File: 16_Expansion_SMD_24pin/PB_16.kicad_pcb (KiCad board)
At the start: 2 copper layers, 148.6 x 75.5 mm, 56 parts, among them J1 String1, J10 String10, J11 String11, J12 String12, J13 String13, J14 String14, J15 String15, J16 String16, J17 Power In Left, J18 Power In Right, J2 String2, J20 v4 Input, J3 String3, J4 String4, J5 String5, J6 String6, J7 String7, J8 String8, J9 String9, U1 74HC245, U2 74HC245

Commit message: added logo
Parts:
- added G***: LOGO, Scotts:chewi_15, F.Cu at (78.4, 112.4)

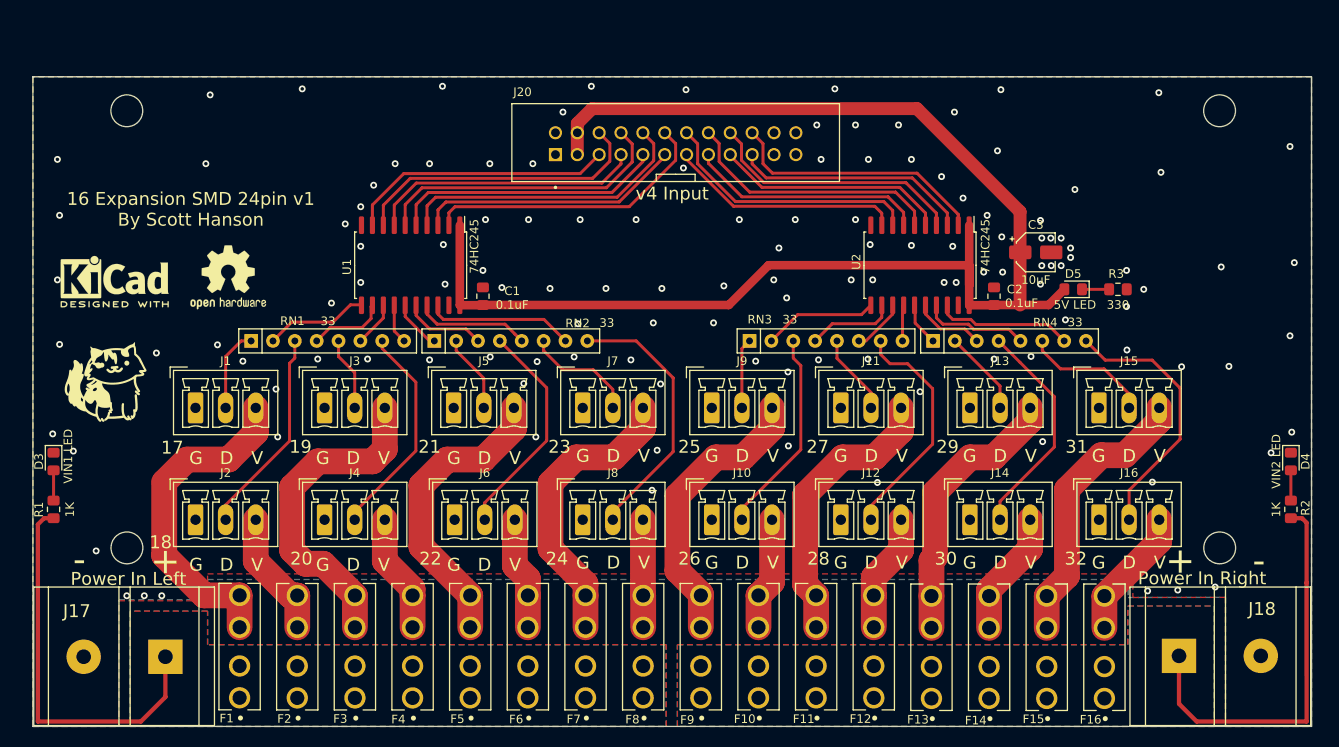
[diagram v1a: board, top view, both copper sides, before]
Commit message: added resistors to help with noise the input lines causing flickering, Updated BOMS
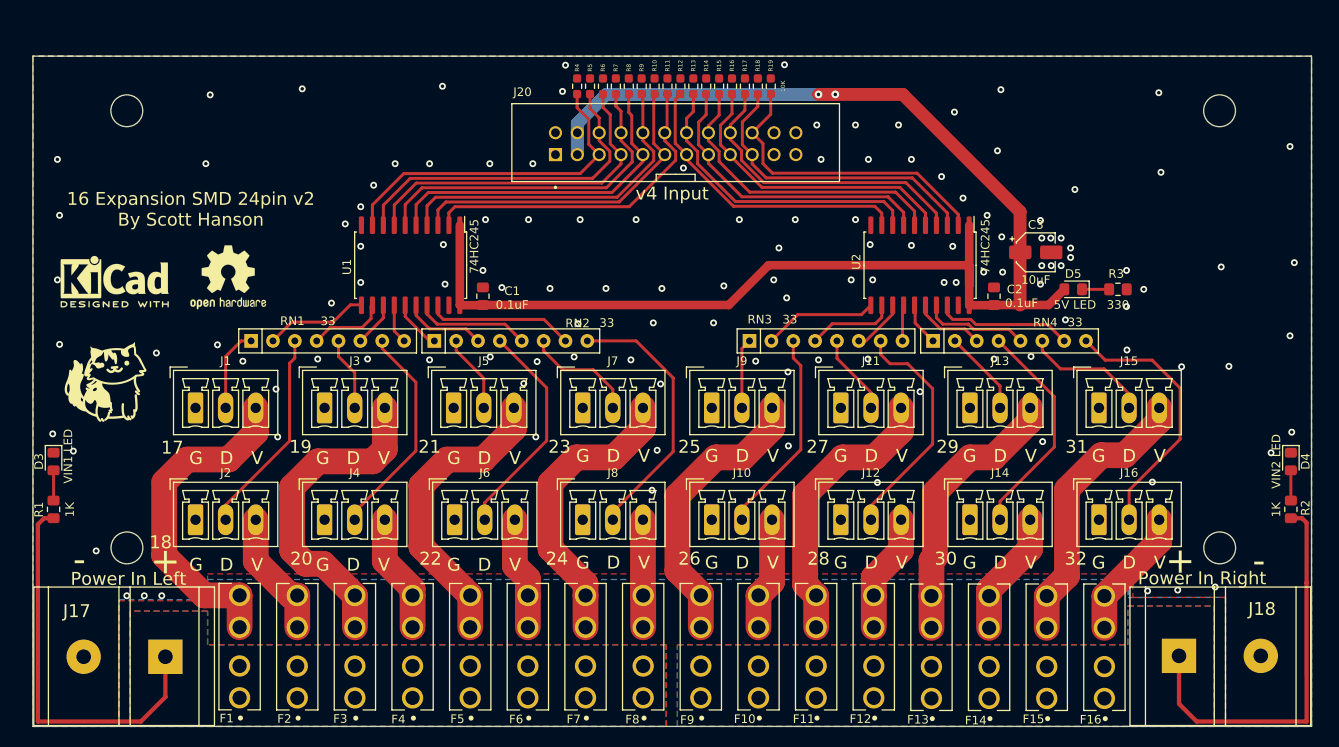
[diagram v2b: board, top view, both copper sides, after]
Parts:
- added R10: 10K, Resistor_SMD:R_0603_1608Metric_Pad0.98x0.95mm_HandSolder, F.Cu at (142.5, 79.2)
- added R11: 10K, Resistor_SMD:R_0603_1608Metric_Pad0.98x0.95mm_HandSolder, F.Cu at (144.0, 79.2)
- added R12: 10K, Resistor_SMD:R_0603_1608Metric_Pad0.98x0.95mm_HandSolder, F.Cu at (145.5, 79.2)
- added R13: 10K, Resistor_SMD:R_0603_1608Metric_Pad0.98x0.95mm_HandSolder, F.Cu at (147.0, 79.2)
- added R14: 10K, Resistor_SMD:R_0603_1608Metric_Pad0.98x0.95mm_HandSolder, F.Cu at (148.5, 79.2)
- added R15: 10K, Resistor_SMD:R_0603_1608Metric_Pad0.98x0.95mm_HandSolder, F.Cu at (150.0, 79.2)
- added R16: 10K, Resistor_SMD:R_0603_1608Metric_Pad0.98x0.95mm_HandSolder, F.Cu at (151.5, 79.2)
- added R17: 10K, Resistor_SMD:R_0603_1608Metric_Pad0.98x0.95mm_HandSolder, F.Cu at (153.0, 79.2)
- added R18: 10K, Resistor_SMD:R_0603_1608Metric_Pad0.98x0.95mm_HandSolder, F.Cu at (154.5, 79.2)
- added R19: 10K, Resistor_SMD:R_0603_1608Metric_Pad0.98x0.95mm_HandSolder, F.Cu at (156.0, 79.2)
- added R4: 10K, Resistor_SMD:R_0603_1608Metric_Pad0.98x0.95mm_HandSolder, F.Cu at (133.5, 79.2)
- added R5: 10K, Resistor_SMD:R_0603_1608Metric_Pad0.98x0.95mm_HandSolder, F.Cu at (135.0, 79.2)
- added R6: 10K, Resistor_SMD:R_0603_1608Metric_Pad0.98x0.95mm_HandSolder, F.Cu at (136.5, 79.2)
- added R7: 10K, Resistor_SMD:R_0603_1608Metric_Pad0.98x0.95mm_HandSolder, F.Cu at (138.0, 79.2)
- added R8: 10K, Resistor_SMD:R_0603_1608Metric_Pad0.98x0.95mm_HandSolder, F.Cu at (139.5, 79.2)
- added R9: 10K, Resistor_SMD:R_0603_1608Metric_Pad0.98x0.95mm_HandSolder, F.Cu at (141.0, 79.2)
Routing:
- net OUT31: track 27.6 -> 35.8 mm
- net OUT17: track 31.1 -> 39.2 mm
- net OUT29: track 27.0 -> 35.0 mm
- net OUT19: track 31.8 -> 39.7 mm
- net OUT27: track 27.6 -> 35.4 mm
- net OUT25: track 27.2 -> 35.1 mm
- net OUT21: track 31.6 -> 39.3 mm
- net OUT23: track 30.9 -> 38.5 mm
- net OUT32: track 30.5 -> 35.9 mm
- net OUT30: track 30.3 -> 35.5 mm
- net OUT28: track 30.6 -> 35.6 mm
- net OUT18: track 34.6 -> 39.5 mm
- net OUT26: track 30.8 -> 35.6 mm
- net OUT20: track 34.8 -> 39.5 mm
- net OUT24: track 34.1 -> 38.7 mm
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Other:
- board size 148.6 x 75.5 mm -> 148.6 x 77.9 mm

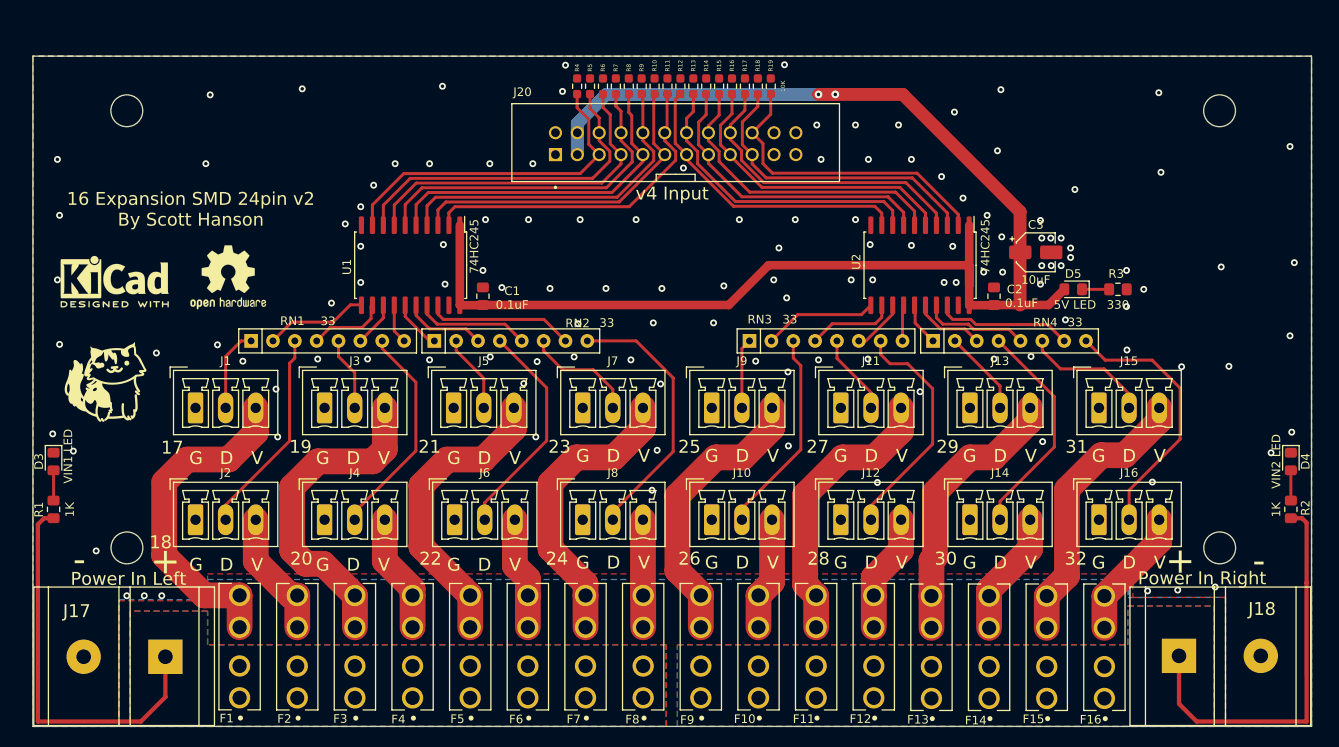
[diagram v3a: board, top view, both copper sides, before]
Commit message: added buffer resistors
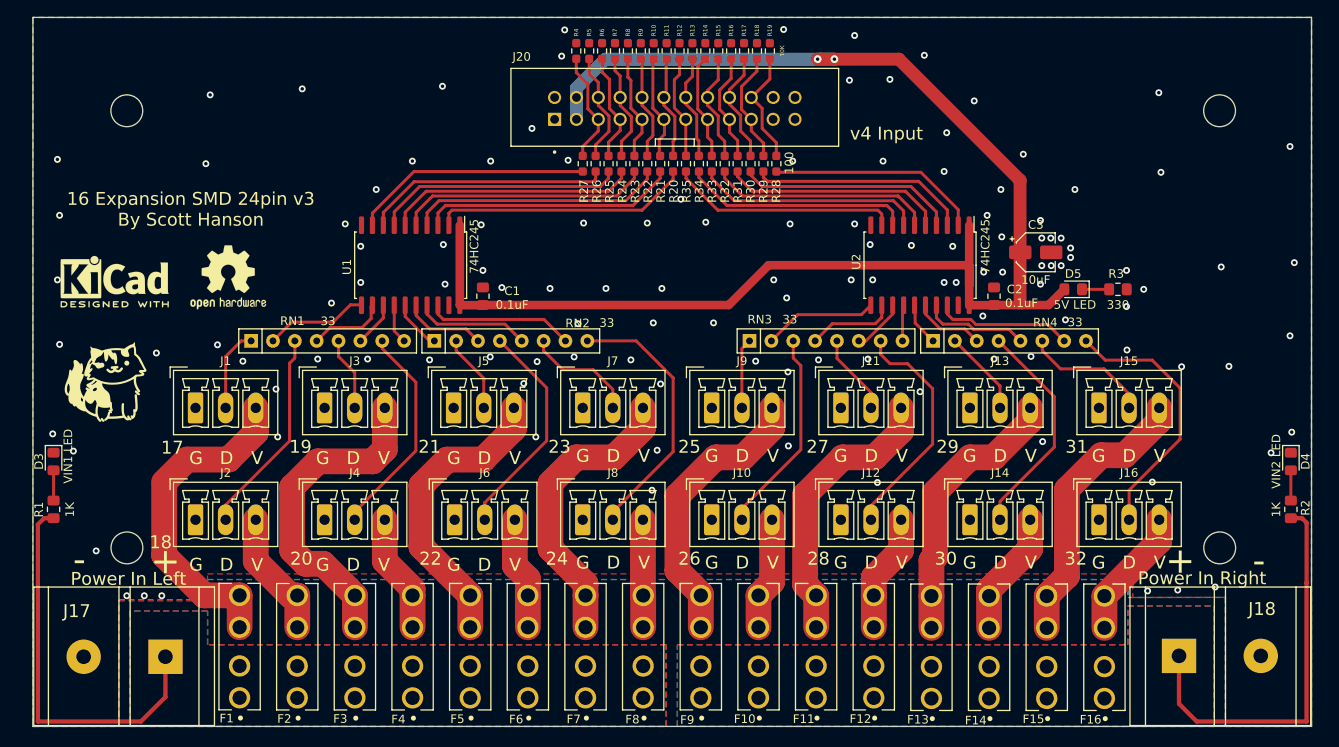
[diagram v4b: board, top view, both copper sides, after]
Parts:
- added R20: 100, Resistor_SMD:R_0603_1608Metric_Pad0.98x0.95mm_HandSolder, F.Cu at (144.6, 88.2)
- added R21: 100, Resistor_SMD:R_0603_1608Metric_Pad0.98x0.95mm_HandSolder, F.Cu at (143.1, 88.2)
- added R22: 100, Resistor_SMD:R_0603_1608Metric_Pad0.98x0.95mm_HandSolder, F.Cu at (141.6, 88.2)
- added R23: 100, Resistor_SMD:R_0603_1608Metric_Pad0.98x0.95mm_HandSolder, F.Cu at (140.1, 88.2)
- added R24: 100, Resistor_SMD:R_0603_1608Metric_Pad0.98x0.95mm_HandSolder, F.Cu at (138.6, 88.2)
- added R25: 100, Resistor_SMD:R_0603_1608Metric_Pad0.98x0.95mm_HandSolder, F.Cu at (137.1, 88.2)
- added R26: 100, Resistor_SMD:R_0603_1608Metric_Pad0.98x0.95mm_HandSolder, F.Cu at (135.6, 88.2)
- added R27: 100, Resistor_SMD:R_0603_1608Metric_Pad0.98x0.95mm_HandSolder, F.Cu at (134.1, 88.2)
- added R28: 100, Resistor_SMD:R_0603_1608Metric_Pad0.98x0.95mm_HandSolder, F.Cu at (156.6, 88.2)
- added R29: 100, Resistor_SMD:R_0603_1608Metric_Pad0.98x0.95mm_HandSolder, F.Cu at (155.1, 88.2)
- added R30: 100, Resistor_SMD:R_0603_1608Metric_Pad0.98x0.95mm_HandSolder, F.Cu at (153.6, 88.2)
- added R31: 100, Resistor_SMD:R_0603_1608Metric_Pad0.98x0.95mm_HandSolder, F.Cu at (152.1, 88.2)
- added R32: 100, Resistor_SMD:R_0603_1608Metric_Pad0.98x0.95mm_HandSolder, F.Cu at (150.6, 88.2)
- added R33: 100, Resistor_SMD:R_0603_1608Metric_Pad0.98x0.95mm_HandSolder, F.Cu at (149.1, 88.2)
- added R34: 100, Resistor_SMD:R_0603_1608Metric_Pad0.98x0.95mm_HandSolder, F.Cu at (147.6, 88.2)
- added R35: 100, Resistor_SMD:R_0603_1608Metric_Pad0.98x0.95mm_HandSolder, F.Cu at (146.1, 88.2)
- moved J20 4.10 mm to (144.8, 81.8)
- moved R10 4.10 mm to (142.4, 75.1)
- moved R11 4.10 mm to (143.9, 75.1)
- moved R12 4.10 mm to (145.4, 75.1)
- moved R13 4.10 mm to (146.9, 75.1)
- moved R14 4.10 mm to (148.4, 75.1)
- moved R15 4.10 mm to (149.9, 75.1)
- moved R16 4.10 mm to (151.4, 75.1)
- moved R17 4.10 mm to (152.9, 75.1)
- moved R18 4.10 mm to (154.4, 75.1)
- moved R19 4.10 mm to (155.9, 75.1)
- moved R4 4.10 mm to (133.4, 75.1)
- moved R5 4.10 mm to (134.9, 75.1)
- moved R6 4.10 mm to (136.4, 75.1)
- moved R7 4.10 mm to (137.9, 75.1)
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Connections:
- U1 pad 2: OUT24 -> Net-(U1-Pad2)
- U1 pad 3: OUT23 -> Net-(U1-Pad3)
- U1 pad 4: OUT22 -> Net-(U1-Pad4)
- U1 pad 5: OUT21 -> Net-(U1-Pad5)
- U1 pad 6: OUT20 -> Net-(U1-Pad6)
- U1 pad 7: OUT19 -> Net-(U1-Pad7)
- U1 pad 8: OUT18 -> Net-(U1-Pad8)
- U1 pad 9: OUT17 -> Net-(U1-Pad9)
- U2 pad 2: OUT32 -> Net-(U2-Pad2)
- U2 pad 3: OUT31 -> Net-(U2-Pad3)
- U2 pad 4: OUT30 -> Net-(U2-Pad4)
- U2 pad 5: OUT29 -> Net-(U2-Pad5)
- U2 pad 6: OUT28 -> Net-(U2-Pad6)
- U2 pad 7: OUT27 -> Net-(U2-Pad7)
- U2 pad 8: OUT26 -> Net-(U2-Pad8)
- U2 pad 9: OUT25 -> Net-(U2-Pad9)
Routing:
- net Net-(U1-Pad2): track 0.00 -> 30.0 mm
- net Net-(U1-Pad3): track 0.00 -> 29.7 mm
- net Net-(U1-Pad4): track 0.00 -> 29.6 mm
- net Net-(U1-Pad5): track 0.00 -> 29.3 mm
- net Net-(U1-Pad6): track 0.00 -> 29.1 mm
- net Net-(U1-Pad7): track 0.00 -> 28.9 mm
- net Net-(U1-Pad8): track 0.00 -> 28.6 mm
- net Net-(U1-Pad9): track 0.00 -> 27.9 mm
- net OUT21: track 39.3 -> 12.3 mm
- net OUT20: track 39.5 -> 12.5 mm
- net OUT22: track 39.1 -> 12.1 mm
- net OUT19: track 39.7 -> 12.7 mm
- net OUT24: track 38.7 -> 12.0 mm
- net OUT18: track 39.5 -> 12.9 mm
- net Net-(U2-Pad9): track 0.00 -> 26.6 mm
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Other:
- board size 148.6 x 77.9 mm -> 148.6 x 82.4 mm

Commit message: update 24pin
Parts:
- removed REF**: OSHW-Logo2_9.8x8mm_SilkScreen, Symbol:OSHW-Logo2_9.8x8mm_SilkScreen
- removed REF**: KiCad-Logo2_5mm_SilkScreen, Symbol:KiCad-Logo2_5mm_SilkScreen
- removed RN1, RN2, RN3, RN4: 33, Resistor_THT:R_Array_SIP8
- C1, C2: footprint Capacitor_SMD:C_0805_2012Metric_Pad1.15x1.40mm_HandSolder -> Capacitor_SMD:C_0402_1005Metric
- D3, D4, D5: footprint LED_SMD:LED_0805_2012Metric_Pad1.15x1.40mm_HandSolder -> LED_SMD:LED_0603_1608Metric
- F1, F10, F11, F12, F13, F14, F15, F16, F2, F3, F4, F5, F6, F7, F8, F9: footprint Keystone_Fuse:FUSE_3544-2 -> Scotts:FUSE_3544-2
- H1, H2, H3, H4: renamed from REF**; value MountingHole_3.7mm -> MountingHole; footprint MountingHole:MountingHole_3.7mm -> Scotts:MountingHole_3.7mm
- J1, J10, J11, J12, J13, J14, J15, J16, J2, J3, J4, J5, J6, J7, J8, J9: footprint Connector_Phoenix_MC:PhoenixContact_MCV_1,5_3-G-3.5_1x03_P3.50mm_Vertical -> Scotts:PhoenixContact_MCV_3.81mm_3.5mm_1x03_Vertical
- R1, R2: value 1K -> 2.2K; footprint Resistor_SMD:R_0805_2012Metric_Pad1.15x1.40mm_HandSolder -> Resistor_SMD:R_0603_1608Metric
- R10, R11, R12, R13, R14, R15, R16, R17, R18, R19, R4, R5, R6, R7, R8, R9: value 10K -> 33ohm; footprint Resistor_SMD:R_0603_1608Metric_Pad0.98x0.95mm_HandSolder -> Resistor_SMD:R_0603_1608Metric
- R20, R21, R22, R23, R24, R25, R26, R27, R28, R29, R30, R31, R32, R33, R34, R35: footprint Resistor_SMD:R_0603_1608Metric_Pad0.98x0.95mm_HandSolder -> Resistor_SMD:R_0603_1608Metric
- R3: footprint Resistor_SMD:R_0805_2012Metric_Pad1.15x1.40mm_HandSolder -> Resistor_SMD:R_0603_1608Metric
- U1, U2: value 74HC245 -> 74HCT541; footprint Package_SO:SOIC-20W_7.5x12.8mm_P1.27mm -> Package_SO:TSSOP-20_4.4x6.5mm_P0.65mm
- moved R4 46.7 mm to (101.1, 108.9), turned to 0 degrees
- moved R5 44.4 mm to (106.0, 108.9), turned to 0 degrees
- moved R19 44.3 mm to (184.5, 108.9), turned to 180 degrees
- moved R18 43.2 mm to (181.3, 108.9), turned to 180 degrees
- moved R6 42.6 mm to (110.4, 108.9), turned to 0 degrees
- moved R17 42.2 mm to (178.1, 108.9), turned to 180 degrees
- moved R7 41.4 mm to (113.9, 108.9), turned to 180 degrees
- moved R16 41.2 mm to (175.0, 108.9), turned to 180 degrees
- moved R8 40.5 mm to (117.0, 108.9), turned to 180 degrees
- moved R15 40.3 mm to (171.9, 108.9), turned to 180 degrees
- moved R14 39.5 mm to (168.7, 108.9), turned to 0 degrees
- moved R9 39.5 mm to (120.5, 108.9), turned to 180 degrees
- moved R10 37.6 mm to (125.8, 108.9), turned to 180 degrees
- moved R13 37.6 mm to (163.3, 108.9), turned to 0 degrees
- moved R11 36.5 mm to (130.0, 108.9), turned to 180 degrees
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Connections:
- R10 pad 1: OUT23 -> /Output 1-8/DOUT7
- R10 pad 2: GND -> Net-(U1-Y1)
- R11 pad 1: OUT24 -> /Output 1-8/DOUT8
- R11 pad 2: GND -> Net-(U1-Y0)
- R12 pad 1: OUT25 -> /Output 9-16/DOUT9
- R12 pad 2: GND -> Net-(U2-Y7)
- R13 pad 1: OUT26 -> /Output 9-16/DOUT10
- R13 pad 2: GND -> Net-(U2-Y6)
- R14 pad 1: OUT27 -> /Output 9-16/DOUT11
- R14 pad 2: GND -> Net-(U2-Y5)
- R15 pad 1: OUT28 -> /Output 9-16/DOUT12
- R15 pad 2: GND -> Net-(U2-Y4)
- R16 pad 1: OUT29 -> /Output 9-16/DOUT13
- R16 pad 2: GND -> Net-(U2-Y3)
- R17 pad 1: OUT30 -> /Output 9-16/DOUT14
- R17 pad 2: GND -> Net-(U2-Y2)
- R18 pad 1: OUT31 -> /Output 9-16/DOUT15
- R18 pad 2: GND -> Net-(U2-Y1)
- R19 pad 1: OUT32 -> /Output 9-16/DOUT16
- R19 pad 2: GND -> Net-(U2-Y0)
- R4 pad 1: OUT17 -> /Output 1-8/DOUT1
- R4 pad 2: GND -> Net-(U1-Y7)
- R5 pad 1: OUT18 -> /Output 1-8/DOUT2
- R5 pad 2: GND -> Net-(U1-Y6)
- R6 pad 1: OUT19 -> /Output 1-8/DOUT3
- R6 pad 2: GND -> Net-(U1-Y5)
- R7 pad 1: OUT20 -> /Output 1-8/DOUT4
- R7 pad 2: GND -> Net-(U1-Y4)
- R8 pad 1: OUT21 -> /Output 1-8/DOUT5
- R8 pad 2: GND -> Net-(U1-Y3)
- R9 pad 1: OUT22 -> /Output 1-8/DOUT6
- R9 pad 2: GND -> Net-(U1-Y2)
- U1 pad 1: +5V -> GND
- U1 pad 11: Net-(RN1-Pad2) -> Net-(U1-Y7)
- U1 pad 12: Net-(RN1-Pad4) -> Net-(U1-Y6)
- U1 pad 13: Net-(RN1-Pad6) -> Net-(U1-Y5)
- U1 pad 14: Net-(RN1-Pad8) -> Net-(U1-Y4)
- U1 pad 15: Net-(RN2-Pad1) -> Net-(U1-Y3)
- U1 pad 16: Net-(RN2-Pad3) -> Net-(U1-Y2)
- U1 pad 17: Net-(RN2-Pad5) -> Net-(U1-Y1)
- U1 pad 18: Net-(RN2-Pad7) -> Net-(U1-Y0)
- U2 pad 1: +5V -> GND
- U2 pad 11: Net-(RN3-Pad2) -> Net-(U2-Y7)
- U2 pad 12: Net-(RN3-Pad4) -> Net-(U2-Y6)
- U2 pad 13: Net-(RN3-Pad6) -> Net-(U2-Y5)
- U2 pad 14: Net-(RN3-Pad8) -> Net-(U2-Y4)
- U2 pad 15: Net-(RN4-Pad1) -> Net-(U2-Y3)
- U2 pad 16: Net-(RN4-Pad3) -> Net-(U2-Y2)
- U2 pad 17: Net-(RN4-Pad5) -> Net-(U2-Y1)
- U2 pad 18: Net-(RN4-Pad7) -> Net-(U2-Y0)
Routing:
- net +5V: track 172.6 -> 138.8 mm, vias 2 -> 0
- net GND: track 0.00 -> 21.7 mm, vias 125 -> 21
- net Net-(U1-Y0): track 0.00 -> 17.2 mm
- net Net-(RN2-Pad7): track 17.1 -> 0.00 mm
- net Net-(RN4-Pad7): track 15.9 -> 0.00 mm
- net Net-(U1-Y1): track 0.00 -> 13.8 mm
- net Net-(U2-Y7): track 0.00 -> 13.8 mm
- net Net-(RN2-Pad5): track 13.3 -> 0.00 mm
- net Net-(RN3-Pad2): track 13.3 -> 0.00 mm
- net Net-(U1-Y7): track 0.00 -> 12.5 mm
- net Net-(U2-Y0): track 0.00 -> 12.4 mm
- net Net-(RN4-Pad5): track 12.3 -> 0.00 mm
- net Net-(RN1-Pad2): track 12.0 -> 0.00 mm
- net Net-(RN3-Pad4): track 10.3 -> 0.00 mm
- net Net-(U2-Y6): track 0.00 -> 9.85 mm
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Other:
- board size 148.6 x 82.4 mm -> 148.6 x 77.4 mm
